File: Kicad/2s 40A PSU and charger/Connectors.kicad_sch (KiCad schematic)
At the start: 19 parts, among them J1 Keystone 3579, J10 USB_C_Receptacle_USB2.0_16P, J11 1.27mm 4 pin socket, J2 JST XH-S Balance Plug, J3 Keystone 3579, J4 Keystone 3569, J5 Keystone 3569, J6 Keystone 3579, J7 Keystone 3579, J8 Keystone 3569, J9 Keystone 3569

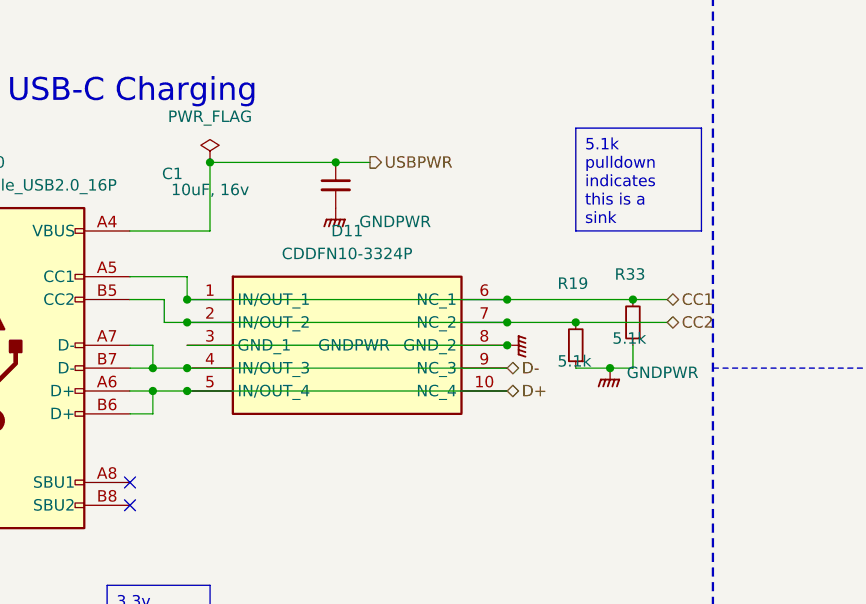
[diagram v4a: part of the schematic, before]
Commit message: Updated Ground connections and tweaked some formatting
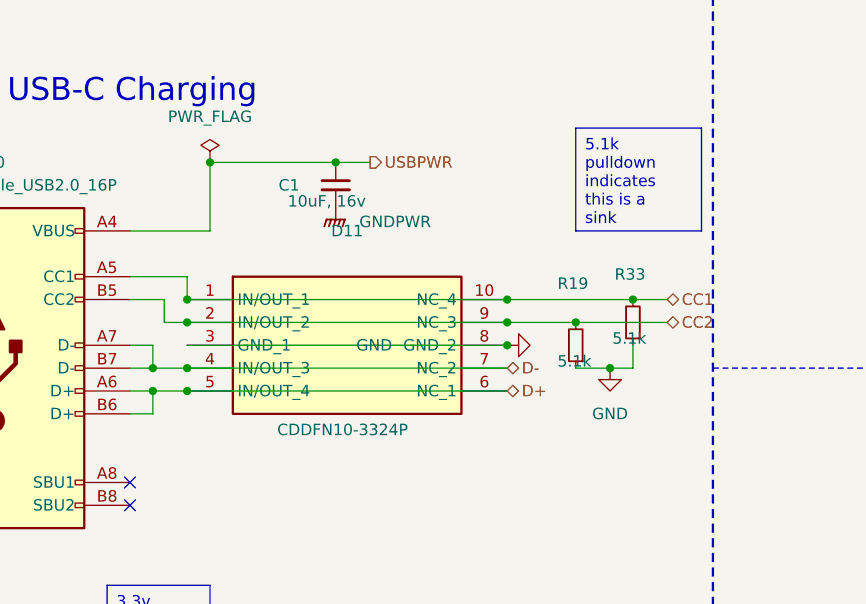
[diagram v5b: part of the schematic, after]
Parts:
- D11: footprint CDDFN10-3324P:CDDFN103324P -> CDDFN103324P
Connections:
- net CC1: now also D11.10 (NC_4); no longer D11.6 (NC_1)
- net CC2: now also D11.9 (NC_3); no longer D11.7 (NC_2)
- net D+: now also D11.6 (NC_1); no longer D11.10 (NC_4)
- net D-: now also D11.7 (NC_2); no longer D11.9 (NC_3)
- net GND: now also D11.3 (GND_1), D11.8 (GND_2), R19.1, R33.1
- net GNDPWR: no longer D11.3 (GND_1), D11.8 (GND_2), R19.1, R33.1
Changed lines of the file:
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@@
 	)
 	(junction
+		(at 124.46 67.31)
+		(diameter 0)
+		(color 0 0 0 0)
+	)
+	(junction
 		(at 68.58 168.91)
 		(diameter 0)
@@
 	)
 	(junction
-		(at 124.46 67.31)
+		(at 55.88 95.25)
 		(diameter 0)
 		(color 0 0 0 0)
 	)
 	(junction
-		(at 55.88 95.25)
+		(at 201.93 95.25)
 		(diameter 0)
 		(color 0 0 0 0)
 	)
 	(junction
-		(at 201.93 95.25)
+		(at 77.47 67.31)
 		(diameter 0)
 		(color 0 0 0 0)
 	)
 	(junction
-		(at 77.47 67.31)
+		(at 113.03 64.77)
 		(diameter 0)
 		(color 0 0 0 0)
@@
 	)
 	(junction
-		(at 113.03 64.77)
-		(diameter 0)
-		(color 0 0 0 0)
-	)
-	(junction
 		(at 73.66 67.31)
 		(diameter 0)
@@
 	(wire
 		(pts
-			(xy 124.46 67.31) (xy 120.65 67.31)
+			(xy 120.65 67.31) (xy 124.46 67.31)
 		)
 		(stroke
@@
 		)
 	)
-	(wire
-		(pts
-			(xy 127 67.31) (xy 124.46 67.31)
-		)
-		(stroke
-			(width 0)
-			(type default)
-		)
-	)
 	(polyline
 		(pts
@@
 	(wire
 		(pts
+			(xy 124.46 67.31) (xy 127 67.31)
+		)
+		(stroke
+			(width 0)
+			(type default)
+		)
+	)
+	(wire
+		(pts
 			(xy 201.93 39.37) (xy 201.93 45.72)
 		)
@@
 	(symbol
 		(lib_id "power:GNDPWR")
-		(at 113.03 64.77 90)
-		(unit 1)
-		(exclude_from_sim no)
-		(in_bom yes)
-		(on_board yes)
-		(dnp no)
-		(property "Reference" "#PWR013"
-			(at 118.11 64.77 0)
-			(effects
-				(font
-					(size 1.27 1.27)
-				)
-				(hide yes)
-			)
-		)
-		(property "Value" "GNDPWR"
-			(at 96.012 64.77 90)
-			(effects
-				(font
-					(size 1.27 1.27)
-				)
-			)
-		)
-		(property "Footprint" ""
-			(at 114.3 64.77 0)
-			(effects
-				(font
-					(size 1.27 1.27)
-				)
-				(hide yes)
-			)
-		)
-		(property "Datasheet" ""
-			(at 114.3 64.77 0)
-			(effects
-				(font
-					(size 1.27 1.27)
-				)
-				(hide yes)
-			)
-		)
-		(property "Description" "Power symbol creates a global label with name \"GNDPWR\" , global ground"
-			(at 113.03 64.77 0)
-			(effects
-				(font
-					(size 1.27 1.27)
-				)
-				(hide yes)
-			)
-		)
-		(pin "1"
-		)
-		(instances
-			(project "2s 40A PSU and charger"
-				(path "/eb3f183d-8bb1-43a5-a363-092ed67891e3/3a3003bc-8e40-4cd7-b859-421f37e4b48c"
-					(reference "#PWR013")
-					(unit 1)
-				)
-			)
-		)
-	)
-	(symbol
-		(lib_id "power:GNDPWR")
 		(at 55.88 97.79 0)
 		(unit 1)
@@
 	)
 	(symbol
+		(lib_id "power:GND")
+		(at 113.03 64.77 90)
+		(unit 1)
+		(exclude_from_sim no)
+		(in_bom yes)
+		(on_board yes)
+		(dnp no)
+		(property "Reference" "#PWR013"
+			(at 119.38 64.77 0)
+			(effects
+				(font
+					(size 1.27 1.27)
+				)
+				(hide yes)
+			)
+		)
+		(property "Value" "GND"
+			(at 96.266 64.77 90)
+			(effects
+				(font
+					(size 1.27 1.27)
+				)
+				(justify right)
+			)
+		)
+		(property "Footprint" ""
+			(at 113.03 64.77 0)
+			(effects
+				(font
+					(size 1.27 1.27)
+				)
+				(hide yes)
+			)
+		)
+		(property "Datasheet" ""
+			(at 113.03 64.77 0)
+			(effects
+				(font
+					(size 1.27 1.27)
+				)
+				(hide yes)
+			)
+		)
+		(property "Description" "Power symbol creates a global label with name \"GND\" , ground"
+			(at 113.03 64.77 0)
+			(effects
+				(font
+					(size 1.27 1.27)
+				)
+				(hide yes)
+			)
+		)
+		(pin "1"
+		)
+		(instances
+			(project "2s 40A PSU and charger"
+				(path "/eb3f183d-8bb1-43a5-a363-092ed67891e3/3a3003bc-8e40-4cd7-b859-421f37e4b48c"
+					(reference "#PWR013")
+					(unit 1)
+				)
+			)
+		)
+	)
+	(symbol
 		(lib_id "power:PWR_FLAG")
 		(at 80.01 44.45 0)
@@
 	)
 	(symbol
+		(lib_id "power:GND")
+		(at 124.46 67.31 0)
+		(unit 1)
+		(exclude_from_sim no)
+		(in_bom yes)
+		(on_board yes)
+		(dnp no)
+		(fields_autoplaced yes)
+		(property "Reference" "#PWR06"
+			(at 124.46 73.66 0)
+			(effects
+				(font
+					(size 1.27 1.27)
+				)
+				(hide yes)
+			)
+		)
+		(property "Value" "GND"
+			(at 124.46 72.39 0)
+			(effects
+				(font
+					(size 1.27 1.27)
+				)
+			)
+		)
+		(property "Footprint" ""
+			(at 124.46 67.31 0)
+			(effects
+				(font
+					(size 1.27 1.27)
+				)
+				(hide yes)
+			)
+		)
+		(property "Datasheet" ""
+			(at 124.46 67.31 0)
+			(effects
+				(font
+					(size 1.27 1.27)
+				)
+				(hide yes)
+			)
+		)
+		(property "Description" "Power symbol creates a global label with name \"GND\" , ground"
+			(at 124.46 67.31 0)
+			(effects
+				(font
+					(size 1.27 1.27)
+				)
+				(hide yes)
+			)
+		)
+		(pin "1"
+		)
+		(instances
+			(project "2s 40A PSU and charger"
+				(path "/eb3f183d-8bb1-43a5-a363-092ed67891e3/3a3003bc-8e40-4cd7-b859-421f37e4b48c"
+					(reference "#PWR06")
+					(unit 1)
+				)
+			)
+		)
+	)
+	(symbol
 		(lib_id "Connector:Conn_01x01_Socket")
 		(at 208.28 151.13 0)
@@
 		(on_board yes)
 		(dnp no)
-		(fields_autoplaced yes)
 		(property "Reference" "D11"
 			(at 95.25 52.07 0)
@@
 		)
 		(property "Value" "CDDFN10-3324P"
-			(at 95.25 54.61 0)
+			(at 94.742 74.168 0)
 			(effects
 				(font
@@
 			)
 		)
-		(property "Footprint" "CDDFN10-3324P:CDDFN103324P"
+		(property "Footprint" "CDDFN103324P"
 			(at 109.22 154.61 0)
 			(effects
@@
 		)
 		(property "Description" "BOURNS - CDDFN10-3324P - DIODE, ESD PROTECTION, 3.3V, 0.45PF"
-			(at 77.47 59.69 0)
+			(at 77.47 58.42 0)
 			(effects
 				(font
@@
 	)
 	(symbol
-		(lib_id "power:GNDPWR")
-		(at 124.46 67.31 0)
-		(unit 1)
-		(exclude_from_sim no)
-		(in_bom yes)
-		(on_board yes)
-		(dnp no)
-		(property "Reference" "#PWR06"
-			(at 124.46 72.39 0)
-			(effects
-				(font
-					(size 1.27 1.27)
-				)
-				(hide yes)
-			)
-		)
-		(property "Value" "GNDPWR"
-			(at 130.302 67.818 0)
-			(effects
-				(font
-					(size 1.27 1.27)
-				)
-			)
-		)
-		(property "Footprint" ""
-			(at 124.46 68.58 0)
-			(effects
-				(font
-					(size 1.27 1.27)
-				)
-				(hide yes)
-			)
-		)
-		(property "Datasheet" ""
-			(at 124.46 68.58 0)
-			(effects
-				(font
-					(size 1.27 1.27)
-				)
-				(hide yes)
-			)
-		)
-		(property "Description" "Power symbol creates a global label with name \"GNDPWR\" , global ground"
-			(at 124.46 67.31 0)
-			(effects
-				(font
-					(size 1.27 1.27)
-				)
-				(hide yes)
-			)
-		)
-		(pin "1"
-		)
-		(instances
-			(project "2s 40A PSU and charger"
-				(path "/eb3f183d-8bb1-43a5-a363-092ed67891e3/3a3003bc-8e40-4cd7-b859-421f37e4b48c"
-					(reference "#PWR06")
-					(unit 1)
-				)
-			)
-		)
-	)
-	(symbol
 		(lib_id "Connector:Conn_01x04_Socket")
 		(at 204.47 34.29 90)
@@
 		(dnp no)
 		(property "Reference" "C1"
-			(at 74.676 45.72 0)
+			(at 87.63 46.99 0)
 			(effects
 				(font
@@
 		)
 		(property "Value" "10uF, 16v"
-			(at 75.692 47.498 0)
+			(at 88.646 48.768 0)
 			(effects
 				(font

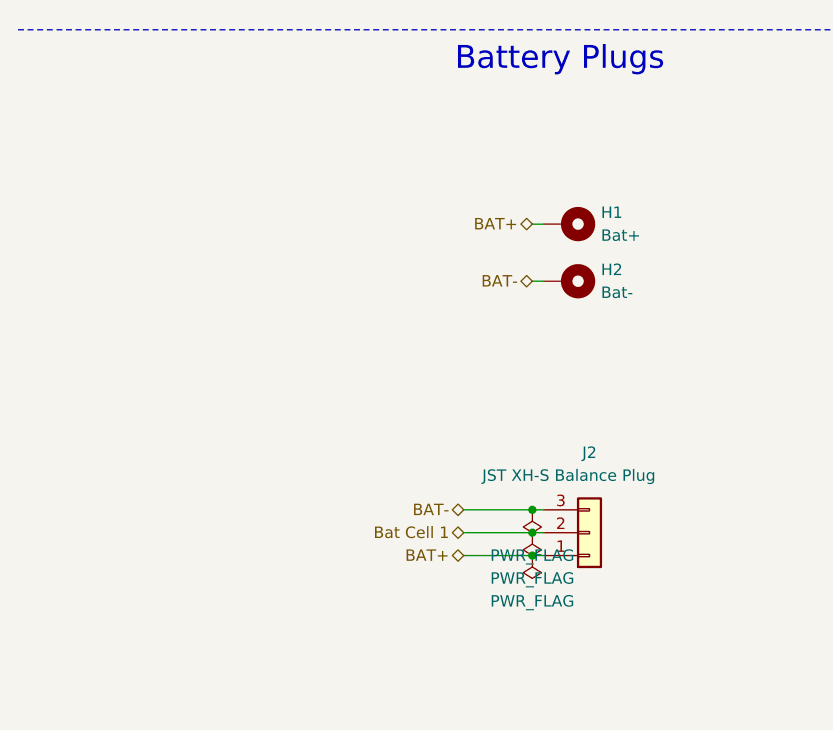
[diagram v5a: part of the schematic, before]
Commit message: Added use of Net Class Directives to speed up routing
I don't have to manually change wire sizes now
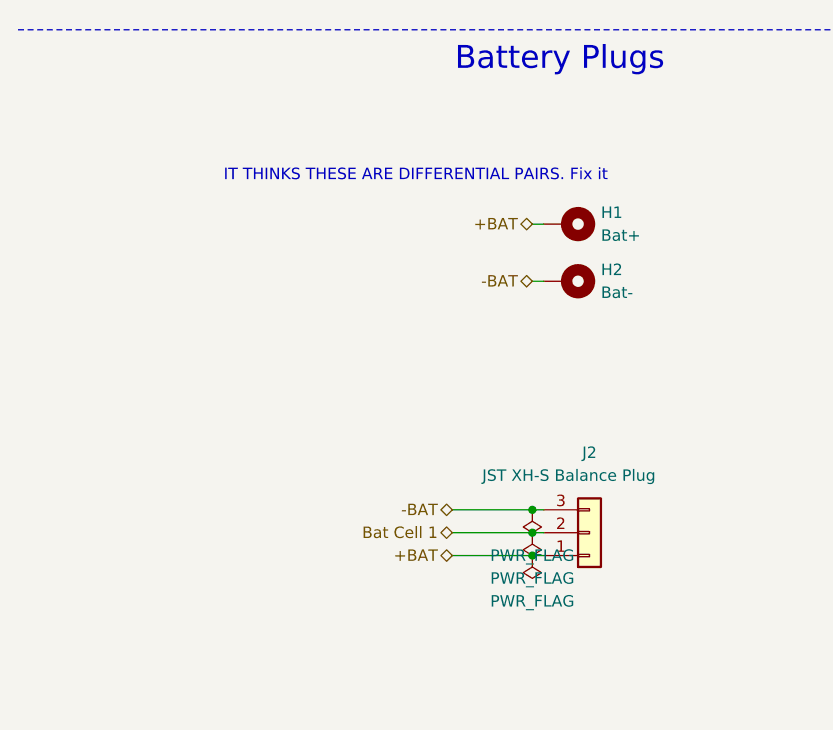
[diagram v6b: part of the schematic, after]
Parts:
- D11: footprint CDDFN103324P -> CDDFN10-3324P:CDDFN103324P
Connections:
- net BAT+ renamed +BAT
- net BAT- renamed -BAT
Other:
- note added: "IT THINKS THESE ARE DIFFERENTIAL PAIRS. Fix it"
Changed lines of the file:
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@@
 	(wire
 		(pts
-			(xy 68.58 163.83) (xy 60.96 163.83)
+			(xy 68.58 163.83) (xy 59.69 163.83)
 		)
 		(stroke
@@
 	(wire
 		(pts
-			(xy 60.96 168.91) (xy 68.58 168.91)
+			(xy 59.69 168.91) (xy 68.58 168.91)
 		)
 		(stroke
@@
 	(wire
 		(pts
-			(xy 60.96 166.37) (xy 68.58 166.37)
+			(xy 59.69 166.37) (xy 68.58 166.37)
 		)
 		(stroke
@@
 			(font
 				(size 2.54 2.54)
+			)
+		)
+	)
+	(text "IT THINKS THESE ARE DIFFERENTIAL PAIRS. Fix it"
+		(exclude_from_sim no)
+		(at 55.626 126.746 0)
+		(effects
+			(font
+				(size 1.27 1.27)
 			)
 		)
@@
 			(justify left)
 		)
+		(property "Netclass" "High Current"
+			(at 203.2 91.44 90)
+			(effects
+				(font
+					(size 1.27 1.27)
+					(italic yes)
+				)
+				(justify left)
+			)
+		)
 	)
 	(hierarchical_label "Bat Cell 1"
 		(shape bidirectional)
-		(at 60.96 166.37 180)
+		(at 59.69 166.37 180)
 		(fields_autoplaced yes)
 		(effects
@@
 			)
 			(justify right)
+		)
+		(property "Netclass" "Logic Power"
+			(at 59.69 167.64 0)
+			(effects
+				(font
+					(size 1.27 1.27)
+					(italic yes)
+				)
+				(justify right)
+				(hide yes)
+			)
 		)
 	)
@@
 		)
 	)
-	(hierarchical_label "BAT+"
+	(hierarchical_label "+BAT"
 		(shape bidirectional)
-		(at 60.96 168.91 180)
+		(at 59.69 168.91 180)
 		(fields_autoplaced yes)
 		(effects
@@
 			(justify right)
 		)
-	)
-	(hierarchical_label "BAT-"
+		(property "Netclass" "High Current"
+			(at 59.69 170.18 0)
+			(effects
+				(font
+					(size 1.27 1.27)
+					(italic yes)
+				)
+				(justify right)
+			)
+		)
+	)
+	(hierarchical_label "-BAT"
 		(shape bidirectional)
 		(at 68.58 138.43 180)
@@
 			)
 			(justify right)
+		)
+		(property "Netclass" "High Current"
+			(at 68.58 139.7 0)
+			(effects
+				(font
+					(size 1.27 1.27)
+					(italic yes)
+				)
+				(justify right)
+			)
 		)
 	)
@@
 			(justify left)
 		)
-	)
-	(hierarchical_label "BAT+"
+		(property "Netclass" "High Current"
+			(at 203.2 133.35 90)
+			(effects
+				(font
+					(size 1.27 1.27)
+					(italic yes)
+				)
+				(justify left)
+			)
+		)
+	)
+	(hierarchical_label "+BAT"
 		(shape bidirectional)
 		(at 68.58 132.08 180)
@@
 			)
 			(justify right)
+		)
+		(property "Netclass" "High Current"
+			(at 68.58 133.35 0)
+			(effects
+				(font
+					(size 1.27 1.27)
+					(italic yes)
+				)
+				(justify right)
+			)
 		)
 	)
@@
 		)
 	)
-	(hierarchical_label "BAT-"
+	(hierarchical_label "-BAT"
 		(shape bidirectional)
-		(at 60.96 163.83 180)
+		(at 59.69 163.83 180)
 		(fields_autoplaced yes)
 		(effects
@@
 			)
 			(justify right)
+		)
+		(property "Netclass" "High Current"
+			(at 59.69 165.1 0)
+			(effects
+				(font
+					(size 1.27 1.27)
+					(italic yes)
+				)
+				(justify right)
+			)
 		)
 	)
@@
 			(justify right)
 		)
+		(property "Netclass" "High Current"
+			(at 198.12 46.99 0)
+			(effects
+				(font
+					(size 1.27 1.27)
+					(italic yes)
+				)
+				(justify right)
+			)
+		)
 	)
 	(hierarchical_label "D+"
@@
 			)
 			(justify left)
+		)
+		(property "Netclass" "USB-C pwr"
+			(at 97.79 45.72 0)
+			(effects
+				(font
+					(size 1.27 1.27)
+					(italic yes)
+				)
+				(justify left)
+			)
 		)
 	)
@@
 			)
 		)
-		(property "Footprint" "CDDFN103324P"
+		(property "Footprint" "CDDFN10-3324P:CDDFN103324P"
 			(at 109.22 154.61 0)
 			(effects

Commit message: Updated Sheet Properties
My author name is now in there, and I've added the proper project name.
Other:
- title: (none) -> CACKLE 2s 40A PSU & Charger
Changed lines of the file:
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@@
 	(paper "A4")
 	(title_block
-		(date "2024-11-28")
-		(rev "V1 Alpha")
+		(title "CACKLE 2s 40A PSU & Charger")
+		(date "2024-12-01")
+		(rev "V1")
+		(comment 1 "Author: Asher Edwards")
 	)
 	(junction

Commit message: Changed battery input pads to through holes with vias
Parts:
- H1, H2: footprint TestPoint:TestPoint_Pad_3.0x3.0mm -> MountingHole:MountingHole_2.2mm_M2_Pad_Via
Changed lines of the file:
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@@
 			)
 		)
-		(property "Footprint" "TestPoint:TestPoint_Pad_3.0x3.0mm"
+		(property "Footprint" "MountingHole:MountingHole_2.2mm_M2_Pad_Via"
 			(at 72.39 138.43 0)
 			(effects
@@
 			)
 		)
-		(property "Footprint" "TestPoint:TestPoint_Pad_3.0x3.0mm"
+		(property "Footprint" "MountingHole:MountingHole_2.2mm_M2_Pad_Via"
 			(at 72.39 132.08 0)
 			(effects
